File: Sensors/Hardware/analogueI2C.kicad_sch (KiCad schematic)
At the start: 60 parts, among them J1 Conn_01x03, J12 Conn_01x03, J13 Conn_01x03, J2 Conn_01x03, J3 Conn_01x03, J4 Conn_01x03, J5 Conn_01x03, J6 Conn_01x03, J7 Conn_01x03, J8 Conn_01x03, U15 ADS1219

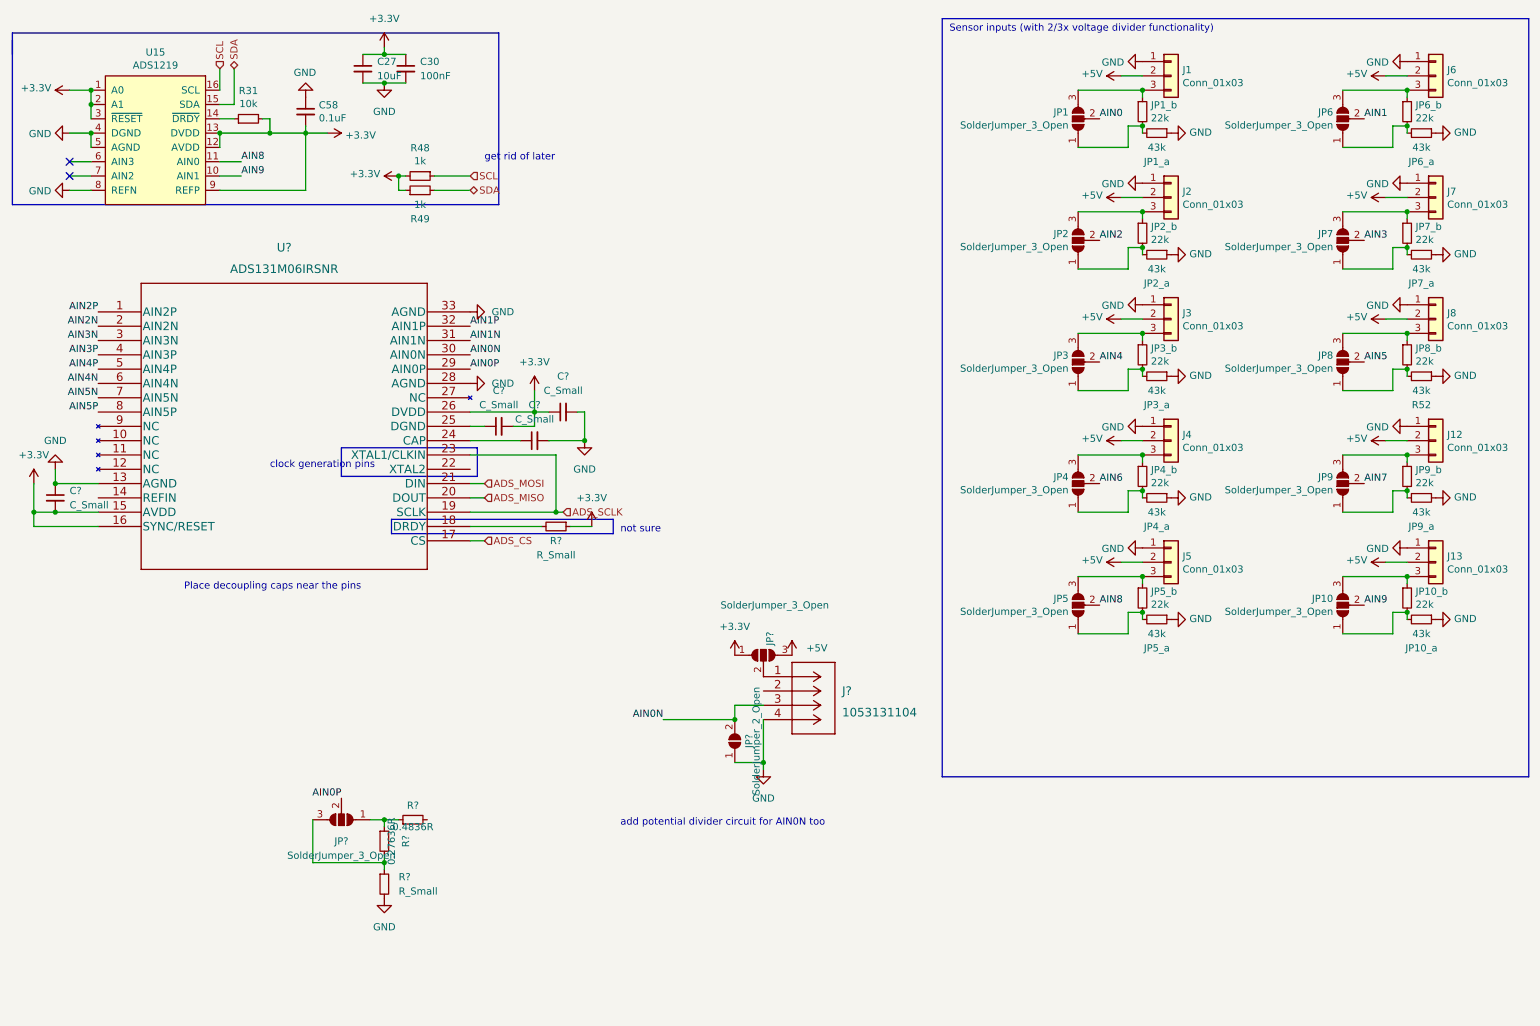
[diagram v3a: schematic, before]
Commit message: values for ADC caps and connector circuits
ADC cap values based on assumptions
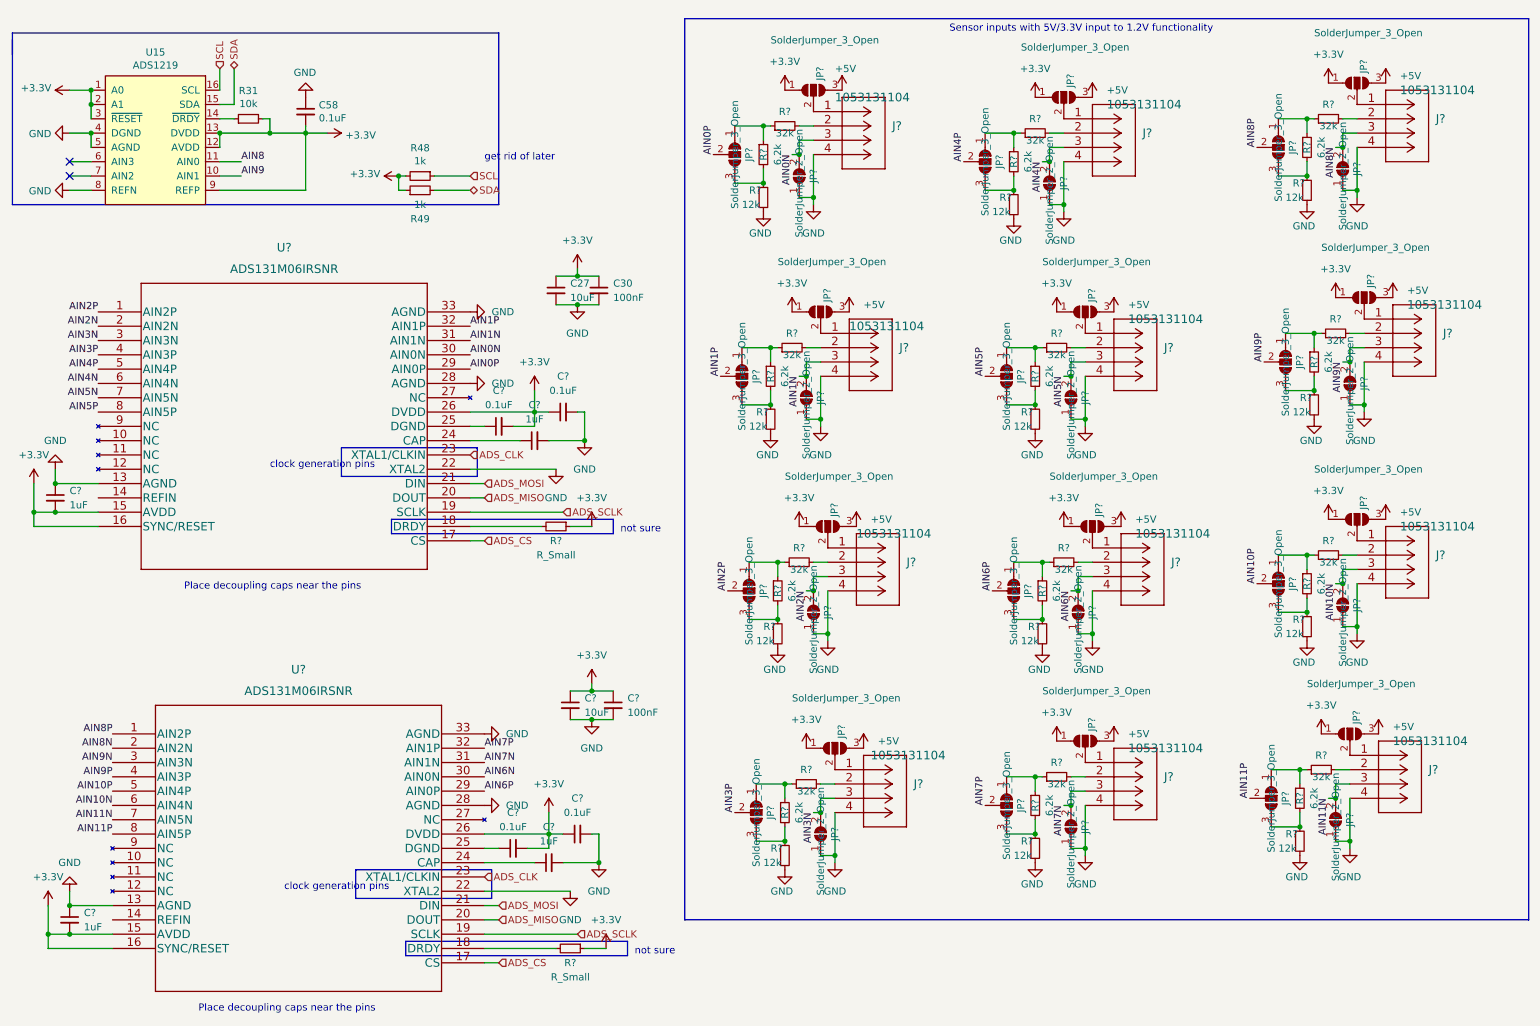
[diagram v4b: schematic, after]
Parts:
- removed J1, J12, J13, J2, J3, J4, J5, J6, J7, J8: Conn_01x03, TerminalBlock_TE-Connectivity:TerminalBlock_TE_282834-3_1x03_P2.54mm_Horizontal, symbol Connector_Generic:Conn_01x03
- removed J?: 1053131104, CON_1053131104, symbol iclr:1053131104
- removed JP1, JP10, JP2, JP3, JP4, JP5, JP6, JP7, JP8, JP9, JP?: SolderJumper_3_Open, Jumper:SolderJumper-3_P1.3mm_Open_RoundedPad1.0x1.5mm_NumberLabels, symbol Jumper:SolderJumper_3_Open
- removed JP10_a, JP1_a, JP2_a, JP3_a, JP4_a, JP5_a, JP6_a, JP7_a, JP9_a, R52: 43k, Resistor_SMD:R_0603_1608Metric, symbol Device:R_Small
- removed JP10_b, JP1_b, JP2_b, JP3_b, JP4_b, JP5_b, JP6_b, JP7_b, JP8_b, JP9_b: 22k, Resistor_SMD:R_0603_1608Metric, symbol Device:R_Small
- removed JP?: SolderJumper_2_Open, symbol Jumper:SolderJumper_2_Open
- removed JP?: SolderJumper_3_Open, symbol Jumper:SolderJumper_3_Open
- removed R?: 0.27636R, symbol Device:R_Small
- removed R?: R_Small, symbol Device:R_Small
- removed R?: 0.4836R, symbol Device:R_Small
- added C? (x2): 1uF, symbol Device:C_Small
- added C?: 100nF, Capacitor_SMD:C_0603_1608Metric, symbol Device:C_Small
- added C? (x2): 0.1uF, symbol Device:C_Small
- added C?: 10uF, Capacitor_SMD:C_0603_1608Metric, symbol Device:C_Small
- added J? (x12): 1053131104, CON_1053131104, symbol iclr:1053131104
- added JP? (x12): SolderJumper_3_Open, Jumper:SolderJumper-3_P1.3mm_Open_RoundedPad1.0x1.5mm_NumberLabels, symbol Jumper:SolderJumper_3_Open
- added JP? (x12): SolderJumper_3_Open, symbol Jumper:SolderJumper_3_Open
- added JP? (x12): SolderJumper_2_Open, symbol Jumper:SolderJumper_2_Open
- added R? (x12): 6.2k, symbol Device:R_Small
- added R? (x12): 12k, symbol Device:R_Small
- added R? (x12): 32k, symbol Device:R_Small
- added R?: R_Small, symbol Device:R_Small
- added U?: ADS131M06IRSNR, QFN_M06IRSNR_TEX, symbol iclr:ADS131M06IRSNR
- C? (x2): value C_Small -> 1uF
- C? (x2): value C_Small -> 0.1uF
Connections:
- net +3V3: now also C?.1, C?.1, C?.1, C?.2, C?.2, JP?.1 (A), JP?.1 (A), JP?.1 (A), JP?.1 (A), JP?.1 (A), JP?.1 (A), JP?.1 (A), JP?.1 (A), JP?.1 (A), JP?.1 (A), JP?.1 (A), JP?.1 (A), R?.1, U?.15 (AVDD), U?.16 (SYNC/RESET), U?.26 (DVDD)
- net +5V: now also JP?.3 (B), JP?.3 (B), JP?.3 (B), JP?.3 (B), JP?.3 (B), JP?.3 (B), JP?.3 (B), JP?.3 (B), JP?.3 (B), JP?.3 (B), JP?.3 (B), JP?.3 (B)
- net ADS_CS: now also U?.17 (CS)
- net ADS_MISO: now also U?.20 (DOUT)
- net ADS_MOSI: now also U?.21 (DIN)
- net ADS_SCLK: now also U?.19 (SCLK); no longer U?.23 (XTAL1/CLKIN)
- net AIN0N: now also J?.3, JP?.2 (B)
- net AIN0P: now also JP?.2 (C)
- net AIN1N: now also J?.3, JP?.2 (B)
- net AIN1P: now also JP?.2 (C)
- net AIN2N: now also J?.3, JP?.2 (B)
- net AIN2P: now also JP?.2 (C)
- net AIN3N: now also J?.3, JP?.2 (B)
- net AIN3P: now also JP?.2 (C)
- net AIN4N: now also J?.3, JP?.2 (B)
- net AIN4P: now also JP?.2 (C)
- net AIN5N: now also J?.3, JP?.2 (B)
- net AIN5P: now also JP?.2 (C)
- net GND: now also U?.22 (XTAL2), C?.1, C?.2, C?.2, C?.2, C?.2, J?.4, J?.4, J?.4, J?.4, J?.4, J?.4, J?.4, J?.4, J?.4, J?.4, J?.4, J?.4, JP?.1 (A), JP?.1 (A), JP?.1 (A), JP?.1 (A), JP?.1 (A), JP?.1 (A), JP?.1 (A), JP?.1 (A), JP?.1 (A), JP?.1 (A), JP?.1 (A), JP?.1 (A), R?.2, R?.2, R?.2, R?.2, R?.2, R?.2, R?.2, R?.2, R?.2, R?.2, R?.2, R?.2, U?.13 (AGND), U?.22 (XTAL2), U?.28 (AGND), U?.33 (AGND)
- new net: JP?.1 (A), R?.1, R?.1 (x12)
- new net: JP?.3 (B), R?.1, R?.2 (x12)
- new net: J?.1, JP?.2 (C) (x12)
- new net: C?.1, U?.24 (CAP)
- new net: J?.2, R?.2 (x12)
- new net: R?.2, U?.18 (DRDY)
- new net: C?.1, U?.25 (DGND)
- new net ADS_CLK: U?.23 (XTAL1/CLKIN), U?.23 (XTAL1/CLKIN)
- new net AIN10N: J?.3, JP?.2 (B), U?.6 (AIN4N)
- new net AIN10P: JP?.2 (C), U?.5 (AIN4P)
- new net AIN11N: J?.3, JP?.2 (B), U?.7 (AIN5N)
- new net AIN11P: JP?.2 (C), U?.8 (AIN5P)
- new net AIN6N: J?.3, JP?.2 (B), U?.30 (AIN0N)
- new net AIN6P: JP?.2 (C), U?.29 (AIN0P)
- new net AIN7N: J?.3, JP?.2 (B), U?.31 (AIN1N)
- new net AIN7P: JP?.2 (C), U?.32 (AIN1P)
- new net AIN8N: J?.3, JP?.2 (B), U?.2 (AIN2N)
- new net AIN8P: JP?.2 (C), U?.1 (AIN2P)
- new net AIN9N: J?.3, JP?.2 (B), U?.3 (AIN3N)
- new net AIN9P: JP?.2 (C), U?.4 (AIN3P)
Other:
- note added: "Sensor inputs with 5V/3.3V input to 1.2V functionality"
- note removed: "Sensor inputs (with 2/3x voltage divider functionality)"
- note removed: "add potential divider circuit for AIN0N too"
- moved on the sheet: C27, C30

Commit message: fixed hierarchical labels and added ref values
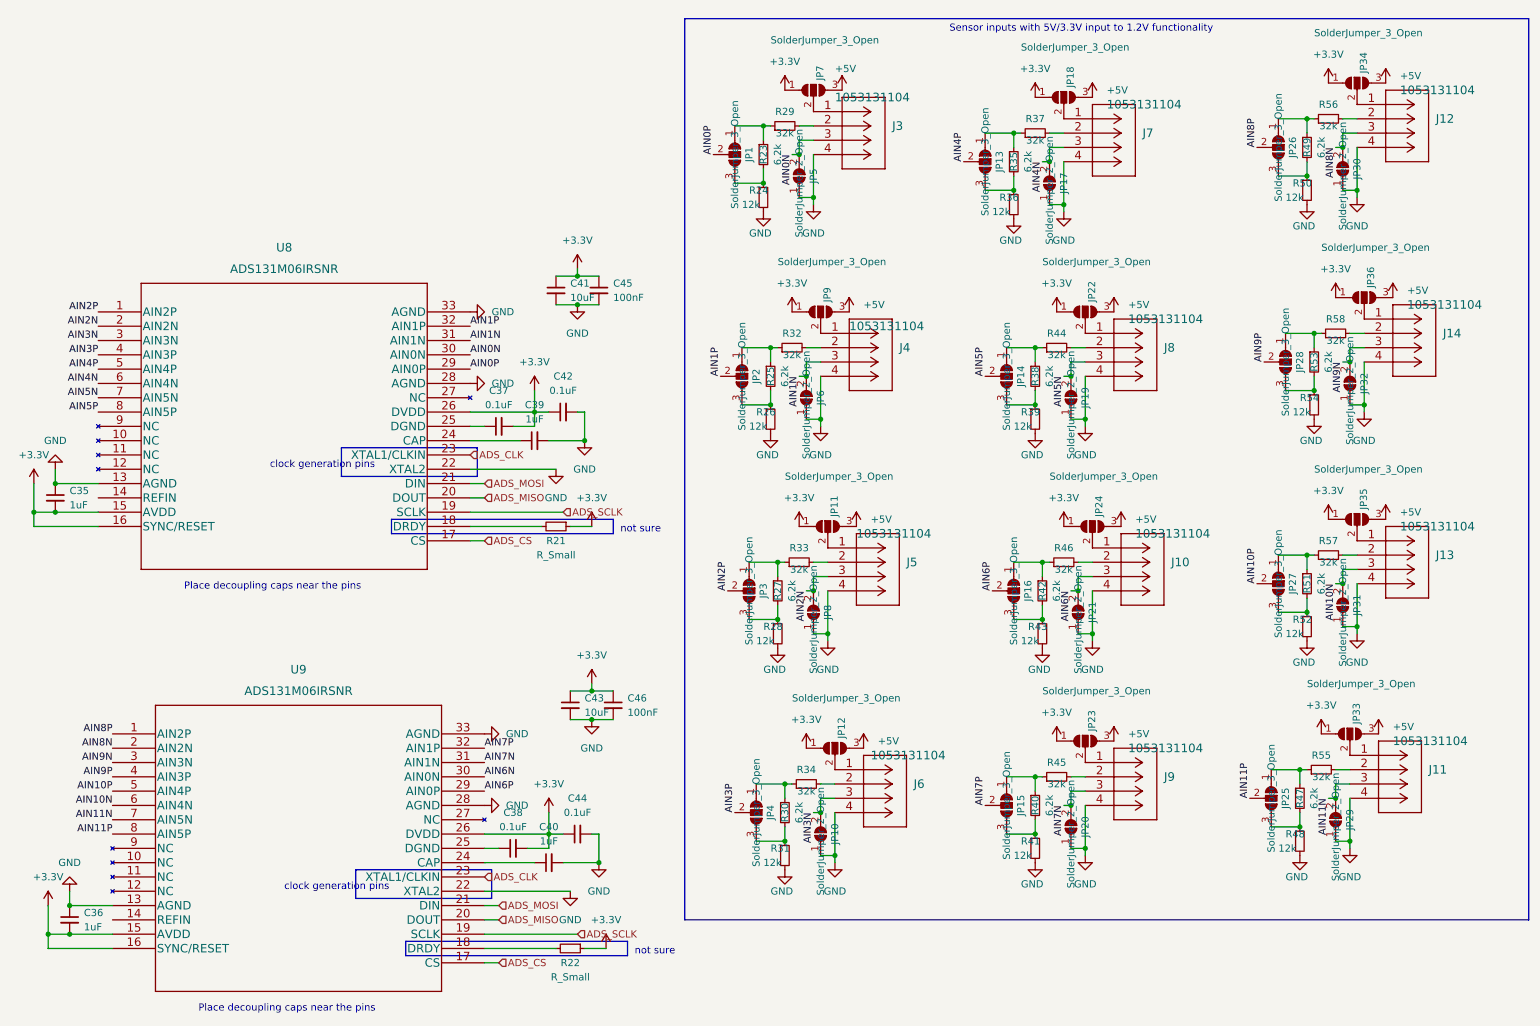
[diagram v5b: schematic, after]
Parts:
- removed C58: 0.1uF, Capacitor_SMD:C_0603_1608Metric, symbol Device:C_Small
- removed R31: 10k, Resistor_SMD:R_0603_1608Metric, symbol Device:R_Small
- removed R48, R49: 1k, Resistor_SMD:R_0603_1608Metric, symbol Device:R_Small
- removed U15: ADS1219, Package_SO:TSSOP-16_4.4x5mm_P0.65mm, symbol iclr:ADS1219
- gave numbers to parts that had none: 98
- renumbered C27 to C41, C30 to C45
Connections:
- no-connect marks 2 -> 0
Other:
- note removed: "get rid of later"

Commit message: added 10V rail, moved to boosts sheet
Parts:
- renumbered C40 to C?, C35 to C?, C46 to C?, C42 to C?, C38 to C?, C37 to C?, C45 to C?, C44 to C?, C43 to C?, C39 to C?, C41 to C?, C36 to C?, J13 to J?, J4 to J?, J8 to J?, J11 to J?, J6 to J?, J14 to J?, J5 to J?, J10 to J?, J3 to J?, J12 to J?, J7 to J?, J9 to J?, JP34 to JP?, JP11 to JP?, JP2 to JP?, JP27 to JP?, JP20 to JP?, JP33 to JP?, JP25 to JP?, JP35 to JP?, JP30 to JP?, JP12 to JP?, JP18 to JP?, JP1 to JP?, JP21 to JP?, JP31 to JP?, JP22 to JP?, JP36 to JP?, JP8 to JP?, JP24 to JP?, JP3 to JP?, JP10 to JP?, JP13 to JP?, JP19 to JP?, JP14 to JP?, JP23 to JP?, JP9 to JP?, JP6 to JP?, JP28 to JP?, JP7 to JP?, JP16 to JP?, JP5 to JP?, JP29 to JP?, JP26 to JP?, JP32 to JP?, JP17 to JP?, JP4 to JP?, JP15 to JP?, R49 to R?, R43 to R?, R48 to R?, R29 to R?, R23 to R?, R31 to R?, R25 to R?, R35 to R?, R58 to R?, R34 to R?, R53 to R?, R40 to R?, R22 to R?, R26 to R?, R37 to R?, R41 to R?, R55 to R?, R32 to R?, R50 to R?, R36 to R?, R54 to R?, R46 to R?, R57 to R?, R38 to R?, R27 to R?, R24 to R?, R33 to R?, R56 to R?, R45 to R?, R52 to R?, R30 to R?, R44 to R?, R47 to R?, R39 to R?, R21 to R?, R28 to R?, R42 to R?, R51 to R?, U8 to U?, U9 to U?
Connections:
- no-connect marks 0 -> 2

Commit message: fp assignments
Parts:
- C39, C40, C41, C42, C43, C44, C46, C48: renamed from C?; footprint (none) -> Capacitor_SMD:C_0402_1005Metric
- C45, C47, C49, C50: renamed from C?; footprint Capacitor_SMD:C_0603_1608Metric -> Capacitor_SMD:C_0402_1005Metric
- JP1, JP13, JP14, JP15, JP16, JP2, JP25, JP26, JP27, JP28, JP3, JP4: renamed from JP?; footprint (none) -> Jumper:SolderJumper-3_P1.3mm_Open_RoundedPad1.0x1.5mm_NumberLabels
- JP10, JP17, JP19, JP20, JP21, JP29, JP30, JP31, JP32, JP5, JP6, JP8: renamed from JP?; footprint (none) -> Jumper:SolderJumper-2_P1.3mm_Open_RoundedPad1.0x1.5mm
- R20, R21: renamed from R?; footprint (none) -> Resistor_SMD:R_0603_1608Metric
- R22, R23, R24, R25, R26, R27, R28, R29, R30, R31, R32, R33, R34, R35, R36, R37, R38, R39, R40, R41, R42, R43, R44, R45, R46, R47, R48, R49, R50, R51, R52, R53, R54, R55, R56, R57: renamed from R?; footprint (none) -> Resistor_SMD:R_0402_1005Metric
- gave numbers to parts that had none: 26
